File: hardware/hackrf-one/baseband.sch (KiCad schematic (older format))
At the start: 134 parts, among them P14 XCVR_CLKOUT, P15 INTR, P16 CLKIN, P18 OEB, P2 CLKOUT, P36 VAA, P37 SCL, P38 SDA, P39 SSP1_SCK, P40 SSP1_MOSI, P41 SSP1_MISO, P53 CS_XCVR, P54 CS_AD, P55 TXENABLE, P56 RXENABLE, P57 XTAL2, P58 GCK1, P59 GCK2, P60 SGPIO_CLK, P61 DA0, P62 DA7, P63 DD0, P64 DD9, P65 DA4, P66 DD5, P67 RSSI, P83 GND, P84 GND, P85 GND, P86 GND, P87 GND, P88 GND, P89 GND, P9 BASEBAND, P90 GND, P91 GND, P92 GND, Q3 MOSFET_P, T3 RX_BALUN, T4 TX_BALUN, U17 MAX2837, U18 MAX5864, U19 SI5351C, X1 GSG-XTAL4PIN

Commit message: 0.2 inch high, 0.1 inch pitch female headers for expansion
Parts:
- P9: Description (none) -> CONN RCPT 16POS .100\" DUAL TIN; Manufacturer (none) -> Samtec; Part Number (none) -> CES-108-01-T-D
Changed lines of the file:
@@
 F 2 "" H 11800 7950 60  0000 C CNN
 F 3 "" H 11800 7950 60  0000 C CNN
+F 4 "Samtec" H 11800 7950 60  0001 C CNN "Manufacturer"
+F 5 "CES-108-01-T-D" H 11800 7950 60  0001 C CNN "Part Number"
+F 6 "CONN RCPT 16POS .100\" DUAL TIN" H 11800 7950 60  0001 C CNN "Description"
 	1    11800 7950
 	1    0    0    -1

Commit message: R16 description corrected
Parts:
- R16: Description RES 4.7KRES 4.7K OHM 1/16W 1% 0402 OHM 1/16W 5% 0402 SMD -> RES 4.7K OHM 1/16W 1% 0402
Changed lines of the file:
@@
 Sheet 3 4
 Title "HackRF One baseband"
-Date "29 nov 2013"
+Date "12 dec 2013"
 Rev ""
 Comp "Copyright 2012 Michael Ossmann"
@@
 F 4 "Stackpole" H 12100 3500 60  0001 C CNN "Manufacturer"
 F 5 "RMCF0402FT4K70" H 12100 3500 60  0001 C CNN "Part Number"
-F 6 "RES 4.7KRES 4.7K OHM 1/16W 1% 0402 OHM 1/16W 5% 0402 SMD" H 12100 3500 60  0001 C CNN "Description"
+F 6 "RES 4.7K OHM 1/16W 1% 0402" H 12100 3500 60  0001 C CNN "Description"
 	1    12100 3500
 	1    0    0    -1

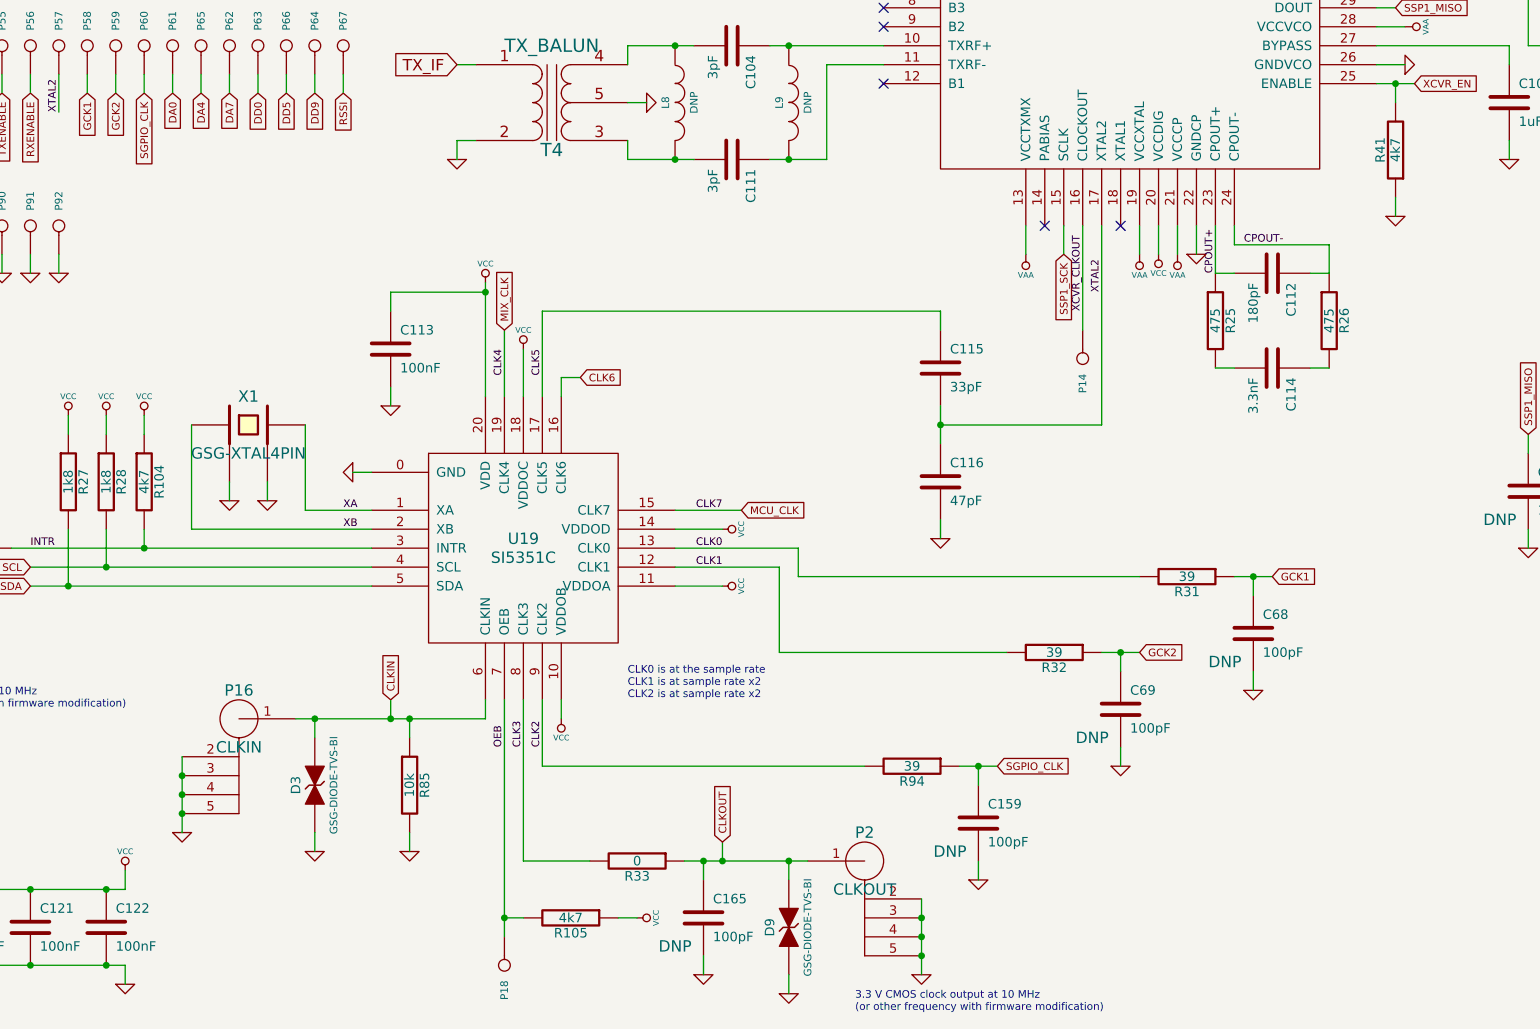
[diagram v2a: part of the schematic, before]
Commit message: changed some 4k7 pull-up or pull-down resistors to 10k to reduce BOM
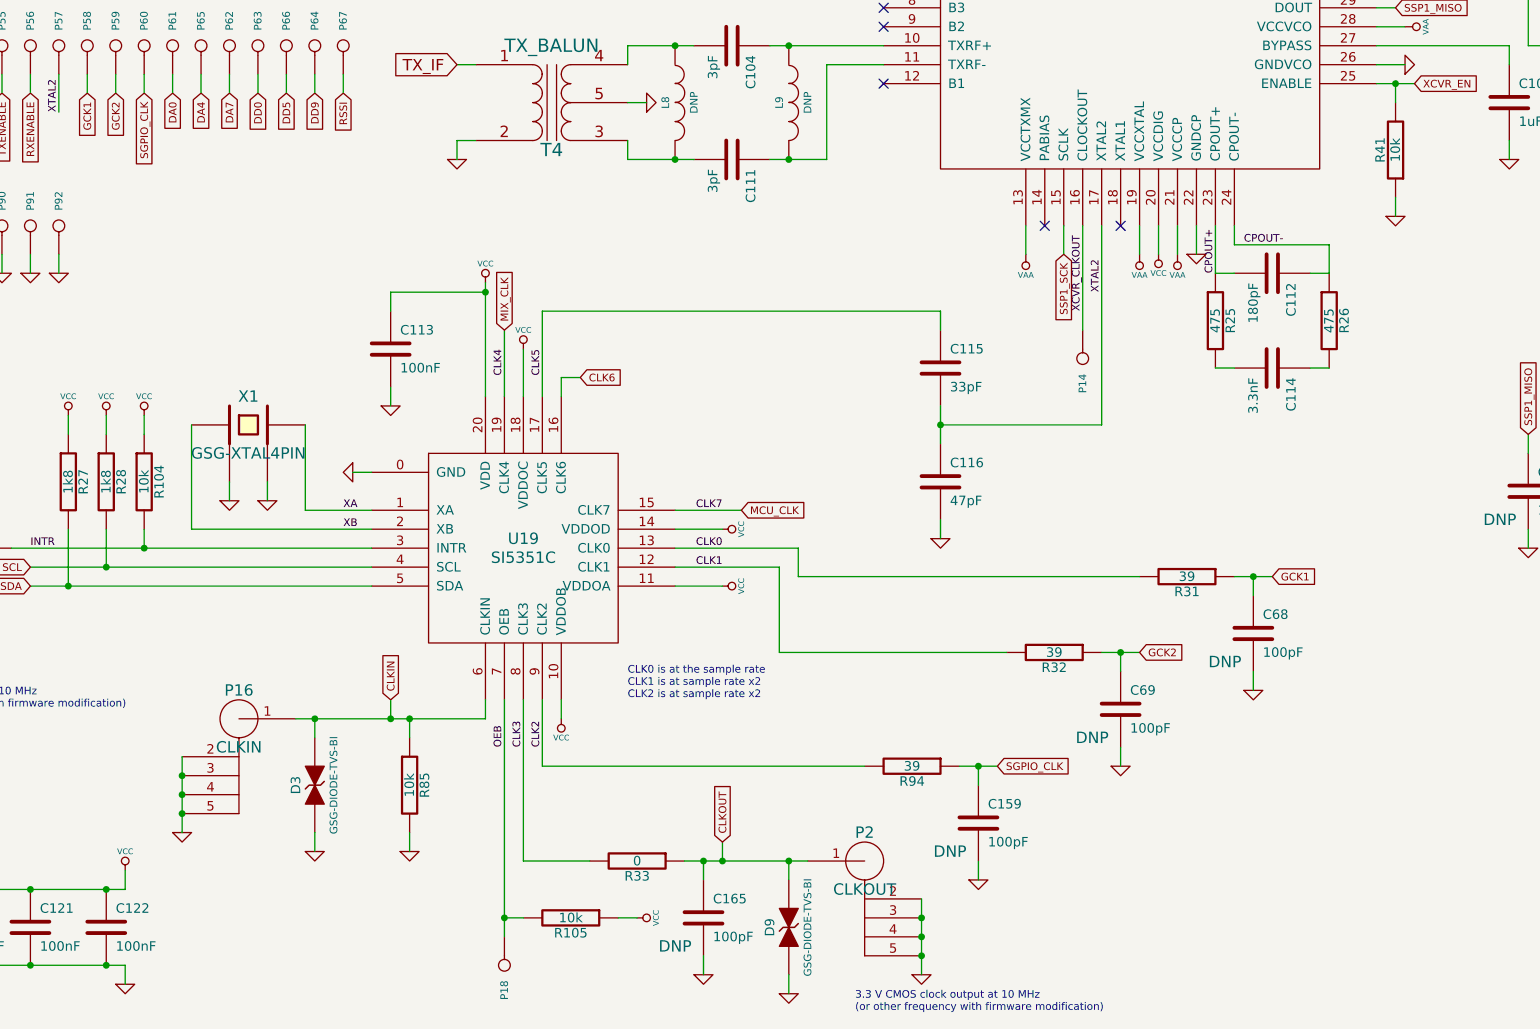
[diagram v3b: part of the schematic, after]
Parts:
- R104, R105, R41: value 4k7 -> 10k; Description RES 4.7K OHM 1/16W 5% 0402 SMD -> RES 10K OHM 1/16W 5% 0402 SMD; Part Number RMCF0402JT4K70 -> RMCF0402JT10K0
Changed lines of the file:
@@
 P 2500 7600
 F 0 "R104" V 2580 7600 50  0000 C CNN
-F 1 "4k7" V 2500 7600 50  0000 C CNN
+F 1 "10k" V 2500 7600 50  0000 C CNN
 F 2 "" H 2500 7600 60  0001 C CNN
 F 3 "" H 2500 7600 60  0001 C CNN
 F 4 "Stackpole" H 2500 7600 60  0001 C CNN "Manufacturer"
-F 5 "RMCF0402JT4K70" H 2500 7600 60  0001 C CNN "Part Number"
-F 6 "RES 4.7K OHM 1/16W 5% 0402 SMD" H 2500 7600 60  0001 C CNN "Description"
+F 5 "RMCF0402JT10K0" H 2500 7600 60  0001 C CNN "Part Number"
+F 6 "RES 10K OHM 1/16W 5% 0402 SMD" H 2500 7600 60  0001 C CNN "Description"
 	1    2500 7600
 	1    0    0    -1
@@
 P 9100 5850
 F 0 "R41" V 9180 5850 50  0000 C CNN
-F 1 "4k7" V 9100 5850 50  0000 C CNN
+F 1 "10k" V 9100 5850 50  0000 C CNN
 F 2 "" H 9100 5850 60  0001 C CNN
 F 3 "" H 9100 5850 60  0001 C CNN
 F 4 "Stackpole" H 9100 5850 60  0001 C CNN "Manufacturer"
-F 5 "RMCF0402JT4K70" H 9100 5850 60  0001 C CNN "Part Number"
-F 6 "RES 4.7K OHM 1/16W 5% 0402 SMD" H 9100 5850 60  0001 C CNN "Description"
+F 5 "RMCF0402JT10K0" H 9100 5850 60  0001 C CNN "Part Number"
+F 6 "RES 10K OHM 1/16W 5% 0402 SMD" H 9100 5850 60  0001 C CNN "Description"
 	1    9100 5850
 	-1   0    0    1
@@
 P 4750 9900
 F 0 "R105" V 4830 9900 50  0000 C CNN
-F 1 "4k7" V 4750 9900 50  0000 C CNN
+F 1 "10k" V 4750 9900 50  0000 C CNN
 F 2 "" H 4750 9900 60  0001 C CNN
 F 3 "" H 4750 9900 60  0001 C CNN
 F 4 "Stackpole" H 4750 9900 60  0001 C CNN "Manufacturer"
-F 5 "RMCF0402JT4K70" H 4750 9900 60  0001 C CNN "Part Number"
-F 6 "RES 4.7K OHM 1/16W 5% 0402 SMD" H 4750 9900 60  0001 C CNN "Description"
+F 5 "RMCF0402JT10K0" H 4750 9900 60  0001 C CNN "Part Number"
+F 6 "RES 10K OHM 1/16W 5% 0402 SMD" H 4750 9900 60  0001 C CNN "Description"
 	1    4750 9900
 	0    1    1    0

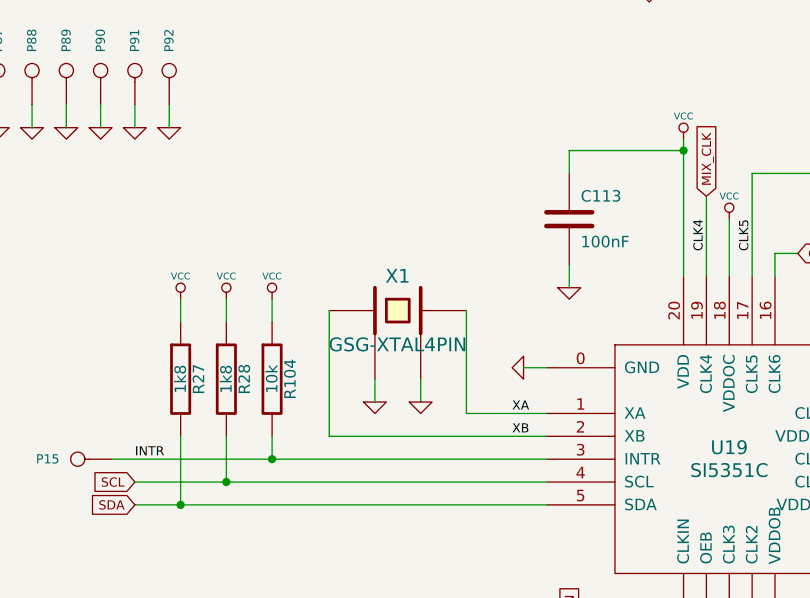
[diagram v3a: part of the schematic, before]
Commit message: load cap footprints for main crystal just in case
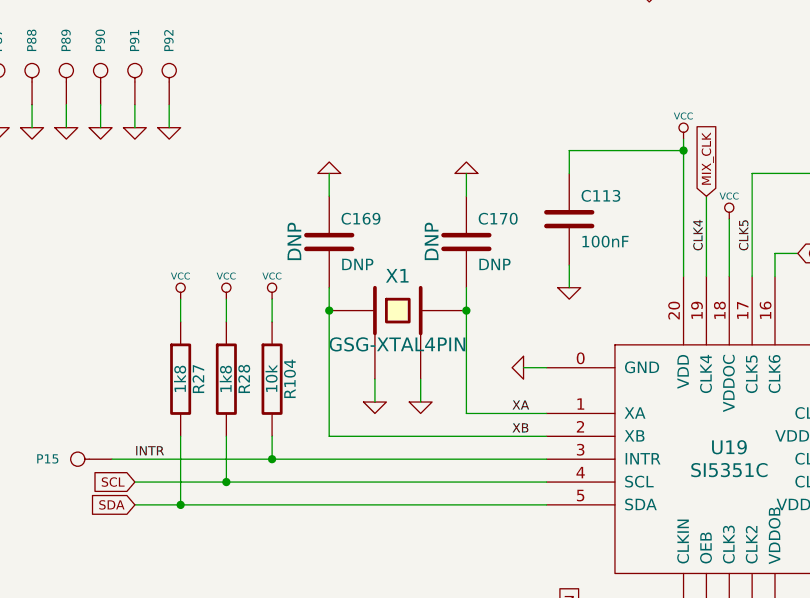
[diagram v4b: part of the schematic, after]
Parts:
- added C169, C170: DNP, symbol C
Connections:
- net GND: now also C169.1, C170.1
- net XA: now also C170.2
- net XB: now also C169.2

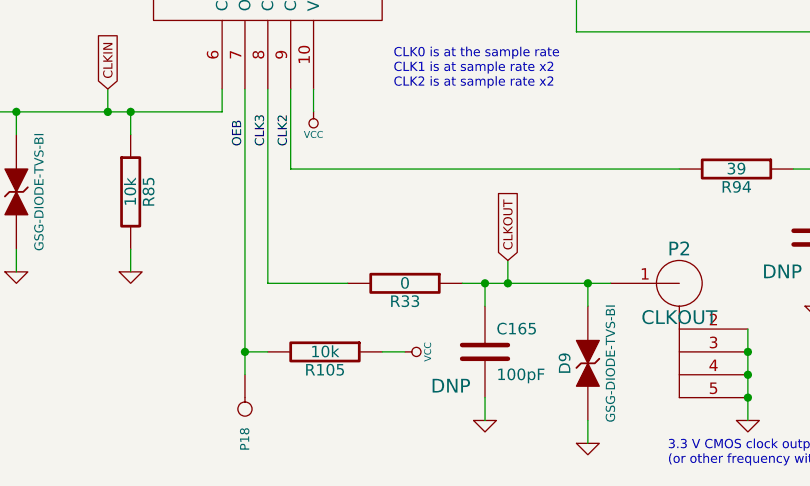
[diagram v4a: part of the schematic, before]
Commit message: series resistance on CLKOUT to reduce overshoot
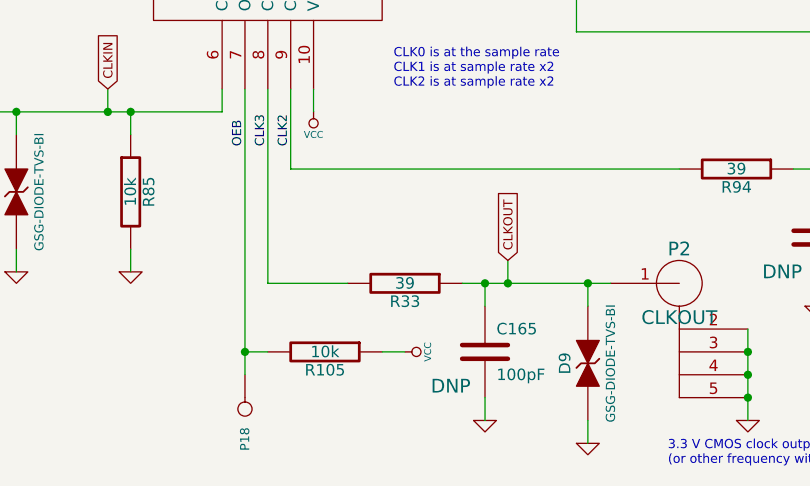
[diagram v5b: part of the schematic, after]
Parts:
- R33: value 0 -> 39; Description RES 0.0 OHM 1/16W 0402 SMD -> RES 39 OHM 1/16W 5% 0402 SMD; Part Number RMCF0402ZT0R00 -> RMCF0402JT39R0
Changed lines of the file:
@@
 P 5100 9600
 F 0 "R33" V 5180 9600 50  0000 C CNN
-F 1 "0" V 5100 9600 50  0000 C CNN
+F 1 "39" V 5100 9600 50  0000 C CNN
 F 2 "" H 5100 9600 60  0001 C CNN
 F 3 "" H 5100 9600 60  0001 C CNN
 F 4 "Stackpole" H 5100 9600 60  0001 C CNN "Manufacturer"
-F 5 "RMCF0402ZT0R00" H 5100 9600 60  0001 C CNN "Part Number"
-F 6 "RES 0.0 OHM 1/16W 0402 SMD" H 5100 9600 60  0001 C CNN "Description"
+F 5 "RMCF0402JT39R0" H 5100 9600 60  0001 C CNN "Part Number"
+F 6 "RES 39 OHM 1/16W 5% 0402 SMD" H 5100 9600 60  0001 C CNN "Description"
 	1    5100 9600
 	0    1    1    0

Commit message: selected 8.5 mm tall (standard) female headers
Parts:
- P9: Description CONN RCPT 16POS .100\" DUAL TIN -> CONN HEADER FMAL 16PS.1\" DL GOLD; Manufacturer Samtec -> Sullins; Part Number CES-108-01-T-D -> PPPC082LFBN-RC
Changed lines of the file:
@@
 Sheet 3 4
 Title "HackRF One baseband"
-Date "12 dec 2013"
+Date "23 dec 2013"
 Rev ""
 Comp "Copyright 2012 Michael Ossmann"
@@
 F 2 "" H 11800 7950 60  0000 C CNN
 F 3 "" H 11800 7950 60  0000 C CNN
-F 4 "Samtec" H 11800 7950 60  0001 C CNN "Manufacturer"
-F 5 "CES-108-01-T-D" H 11800 7950 60  0001 C CNN "Part Number"
-F 6 "CONN RCPT 16POS .100\" DUAL TIN" H 11800 7950 60  0001 C CNN "Description"
+F 4 "Sullins" H 11800 7950 60  0001 C CNN "Manufacturer"
+F 5 "PPPC082LFBN-RC" H 11800 7950 60  0001 C CNN "Part Number"
+F 6 "CONN HEADER FMAL 16PS.1\" DL GOLD" H 11800 7950 60  0001 C CNN "Description"
 	1    11800 7950
 	1    0    0    -1

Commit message: changed to a different SMA connector for physical strength and enclosure compatibility
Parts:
- P16, P2: symbol GSG-SMA-CONN -> GSG-RF-CONN
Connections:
- net GND: no longer P16.3 (GND), P16.4 (GND), P16.5 (GND), P2.3 (GND), P2.4 (GND), P2.5 (GND)
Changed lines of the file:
@@
 Sheet 3 4
 Title "HackRF One baseband"
-Date "23 dec 2013"
+Date "10 jan 2014"
 Rev ""
 Comp "Copyright 2012 Michael Ossmann"
@@
 $EndComp
 $Comp
-L GSG-SMA-CONN P2
+L GSG-RF-CONN P2
 U 1 1 50462549
 P 6300 9600
@@
 L GND #PWR184
 U 1 1 50462548
-P 6600 10200
-F 0 "#PWR184" H 6600 10200 30  0001 C CNN
-F 1 "GND" H 6600 10130 30  0001 C CNN
-F 2 "" H 6600 10200 60  0001 C CNN
-F 3 "" H 6600 10200 60  0001 C CNN
-	1    6600 10200
+P 6300 10100
+F 0 "#PWR184" H 6300 10100 30  0001 C CNN
+F 1 "GND" H 6300 10030 30  0001 C CNN
+F 2 "" H 6300 10100 60  0001 C CNN
+F 3 "" H 6300 10100 60  0001 C CNN
+	1    6300 10100
 	1    0    0    -1
 $EndComp
@@
 L GND #PWR177
 U 1 1 4F5D1728
-P 2700 9450
-F 0 "#PWR177" H 2700 9450 30  0001 C CNN
-F 1 "GND" H 2700 9380 30  0001 C CNN
-F 2 "" H 2700 9450 60  0001 C CNN
-F 3 "" H 2700 9450 60  0001 C CNN
-	1    2700 9450
+P 3000 9350
+F 0 "#PWR177" H 3000 9350 30  0001 C CNN
+F 1 "GND" H 3000 9280 30  0001 C CNN
+F 2 "" H 3000 9350 60  0001 C CNN
+F 3 "" H 3000 9350 60  0001 C CNN
+	1    3000 9350
 	1    0    0    -1
 $EndComp
 $Comp
-L GSG-SMA-CONN P16
+L GSG-RF-CONN P16
 U 1 1 4F5D16D6
 P 3000 8850
@@
 Wire Wire Line
 	14200 3750 14200 2700
-Connection ~ 2700 9150
 Wire Wire Line
 	7550 6250 7550 7300
@@
 Wire Wire Line
 	4500 9900 4400 9900
-Connection ~ 2700 9250
 Wire Wire Line
 	3150 7600 3150 7700
@@
 Wire Wire Line
 	2950 7700 2950 7600
-Connection ~ 2700 9350
-Wire Wire Line
-	2700 9050 2700 9450
 Wire Wire Line
 	5000 9900 5100 9900
@@
 	4600 9100 4600 8750
 Wire Wire Line
-	6600 9800 6600 10200
-Connection ~ 6600 10100
-Connection ~ 6600 10000
-Connection ~ 6600 9900
-Wire Wire Line
 	4400 6800 4400 7150
 Wire Wire Line
@@
 Connection ~ 2750 7300
 Connection ~ 3350 7300
+Wire Wire Line
+	6300 10000 6300 10100
+Wire Wire Line
+	3000 9250 3000 9350
 $EndSCHEMATC

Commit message: bom update for new SMA connectors
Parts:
- P16, P2: Description CONN SMA JACK 50 OHM EDGE MNT -> CONN SMA JACK 50 OHM EDGE MNT W/JAM NUT & LOCK WASHER; Manufacturer Linx Technologies -> Molex; Part Number CONSMA003.062 -> 73251-2121
